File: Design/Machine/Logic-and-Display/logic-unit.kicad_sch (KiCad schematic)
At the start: 10 parts, among them J2 RJ45, K1 SRD-12VDC-SL-C, K2 SRD-12VDC-SL-C, K3 SRD-12VDC-SL-C, K4 SRD-12VDC-SL-C, SW1 ToggleAutoPoints, SW2 SynchRemote, U4 ESP32_NODEMCU, U5 NRF24L01_Breakout

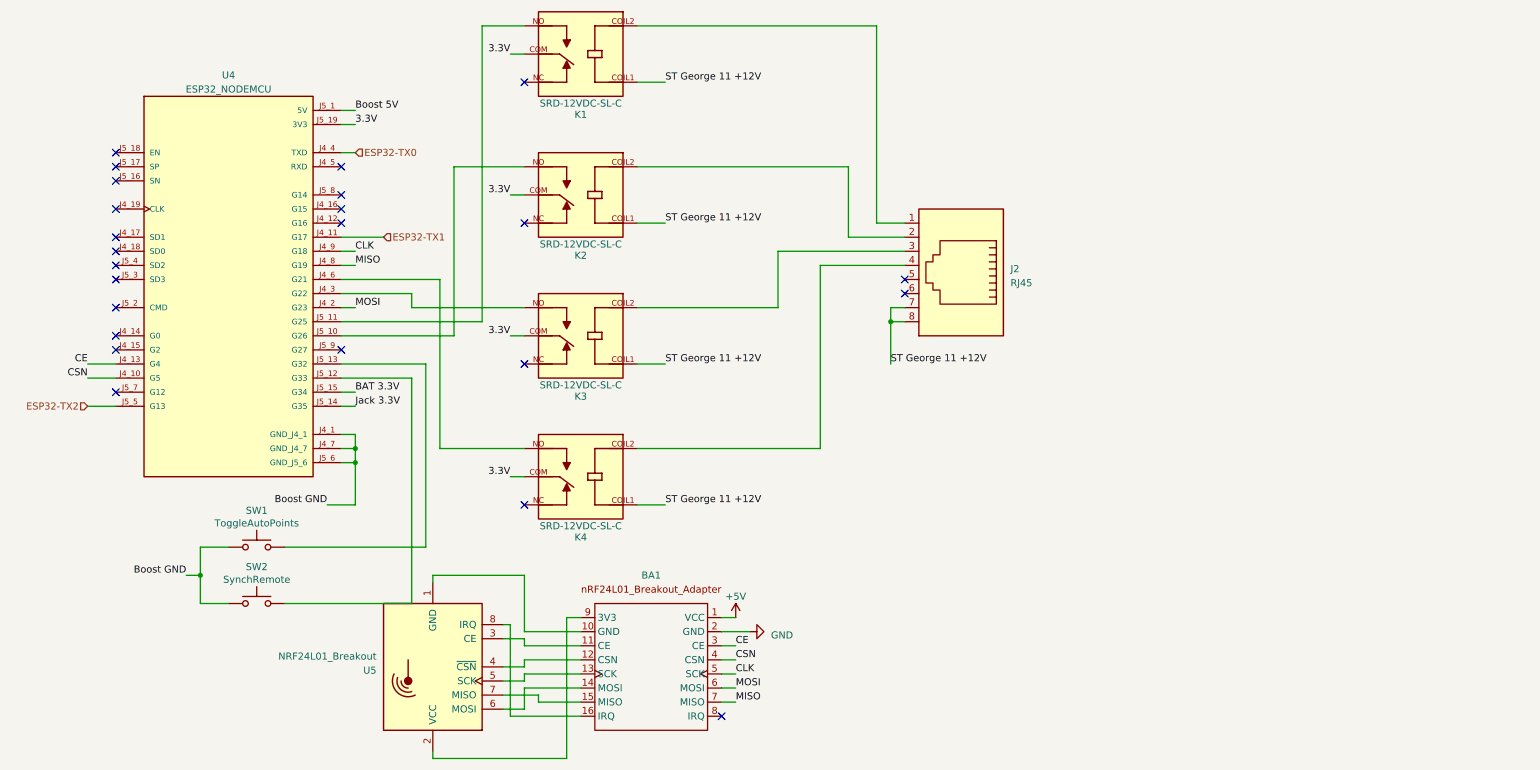
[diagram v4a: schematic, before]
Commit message: feat: logic and display units schecmatics
complete logic and display units schematics
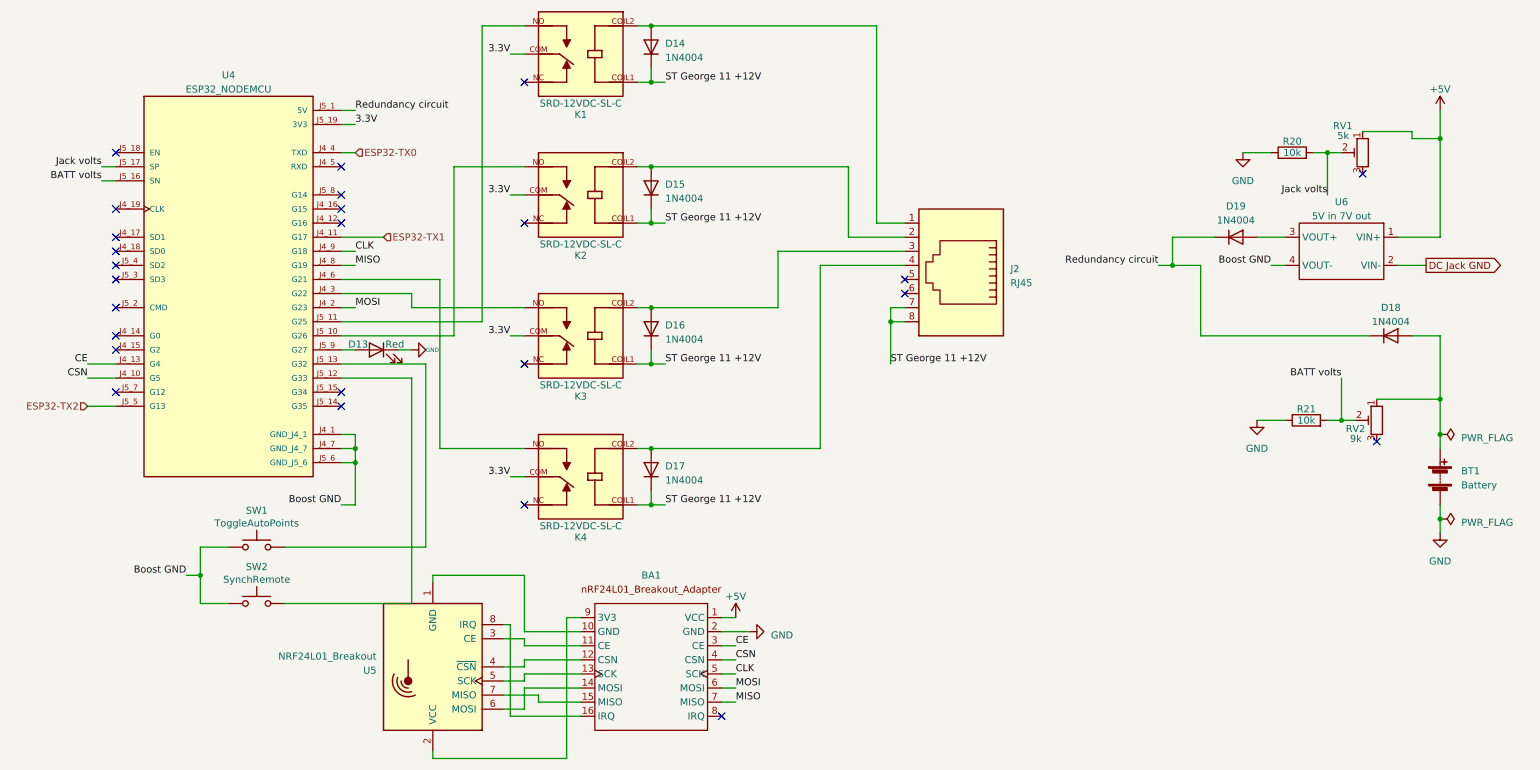
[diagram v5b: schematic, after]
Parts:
- added BT1: Battery, Connector_PinSocket_2.54mm:PinSocket_1x02_P2.54mm_Vertical, symbol Device:Battery
- added D13: Red, Connector_PinSocket_2.54mm:PinSocket_1x02_P2.54mm_Vertical, symbol Device:LED
- added D14, D15, D16, D17, D18, D19: 1N4004, Diode_THT:D_DO-41_SOD81_P10.16mm_Horizontal, symbol Diode:1N4004
- added R20, R21: 10k, Resistor_THT:R_Axial_DIN0309_L9.0mm_D3.2mm_P15.24mm_Horizontal, symbol Device:R
- added RV1: 5k, Connector_PinSocket_2.54mm:PinSocket_1x03_P2.54mm_Vertical, symbol Device:R_Potentiometer_Trim
- added RV2: 9k, Connector_PinSocket_2.54mm:PinSocket_1x03_P2.54mm_Vertical, symbol Device:R_Potentiometer_Trim
- added U6: 5V in 7V out, Connector_PinHeader_2.54mm:PinHeader_1x04_P2.54mm_Vertical, symbol Arduino modules:MT3608_step_up
- SW1, SW2: footprint Button_Switch_THT:SW_PUSH_6mm -> Connector_PinSocket_2.54mm:PinSocket_1x02_P2.54mm_Vertical
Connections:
- net +5V: now also RV1.1, U6.1 (VIN+)
- net Boost GND: now also U6.4 (VOUT-)
- net GND: now also BT1.2 (-), D13.1 (K), R20.1, R21.1
- net ST George 11 +12V: now also D14.1 (K), D15.1 (K), D16.1 (K), D17.1 (K)
- net at J2.1, K1.COIL2: now also D14.2 (A)
- net at J2.4, K4.COIL2: now also D17.2 (A)
- net BATT volts: now reaches U4.J5_16 (SN)
- net BATT volts: now also R21.2, RV2.2
- net Jack volts: now reaches U4.J5_17 (SP)
- net Jack volts: now also R20.2, RV1.2
- net at U4.J5_9 (G27): now also D13.2 (A)
- net at J2.2, K2.COIL2: now also D15.2 (A)
- net at J2.3, K3.COIL2: now also D16.2 (A)
- net BAT 3.3V: no longer names the net of U4.J5_15 (G34)
- net Boost 5V renamed Redundancy circuit
- net Redundancy circuit: now also D18.1 (K), D19.1 (K)
- net Jack 3.3V: no longer names the net of U4.J5_14 (G35)
- new net: D19.2 (A), U6.3 (VOUT+)
- new net: BT1.1 (+), D18.2 (A), RV2.1
- new net DC Jack GND: U6.2 (VIN-)
- no-connect marks 24 -> 25

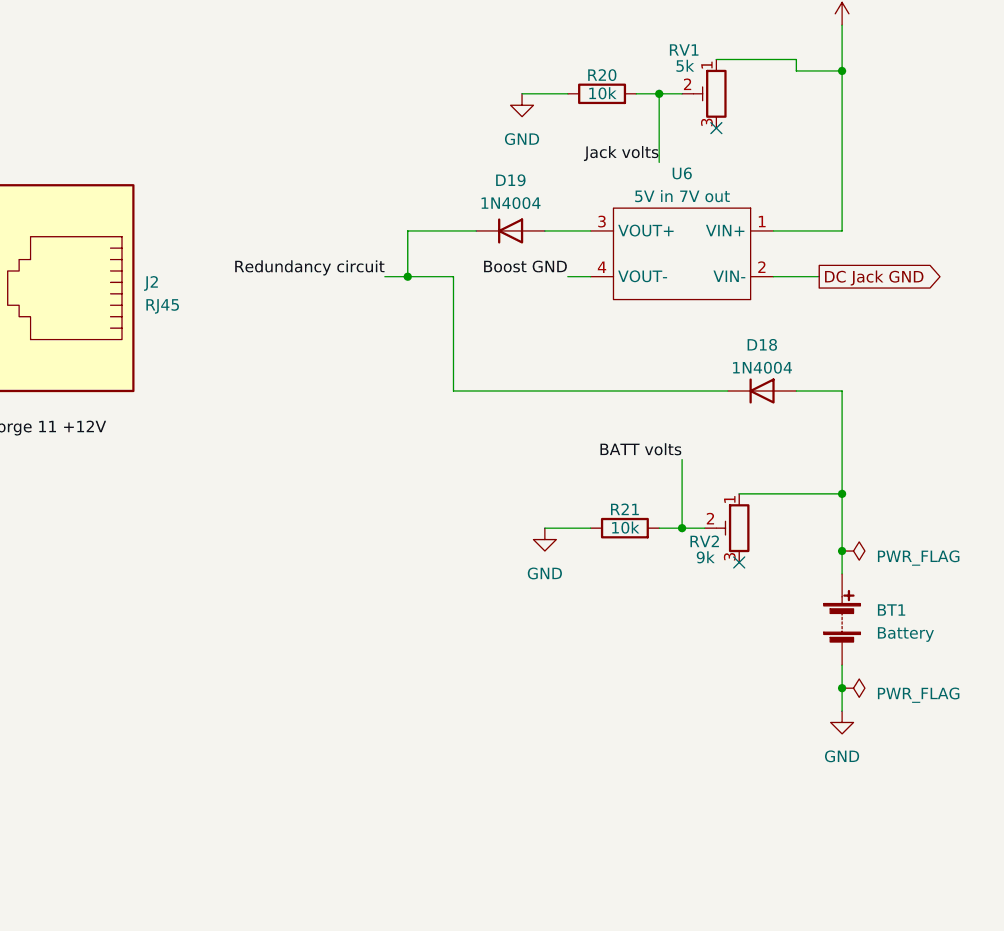
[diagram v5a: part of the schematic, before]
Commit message: fix: logic and display units on/off switch
include a DPST switch to disconnect battery and DC jack
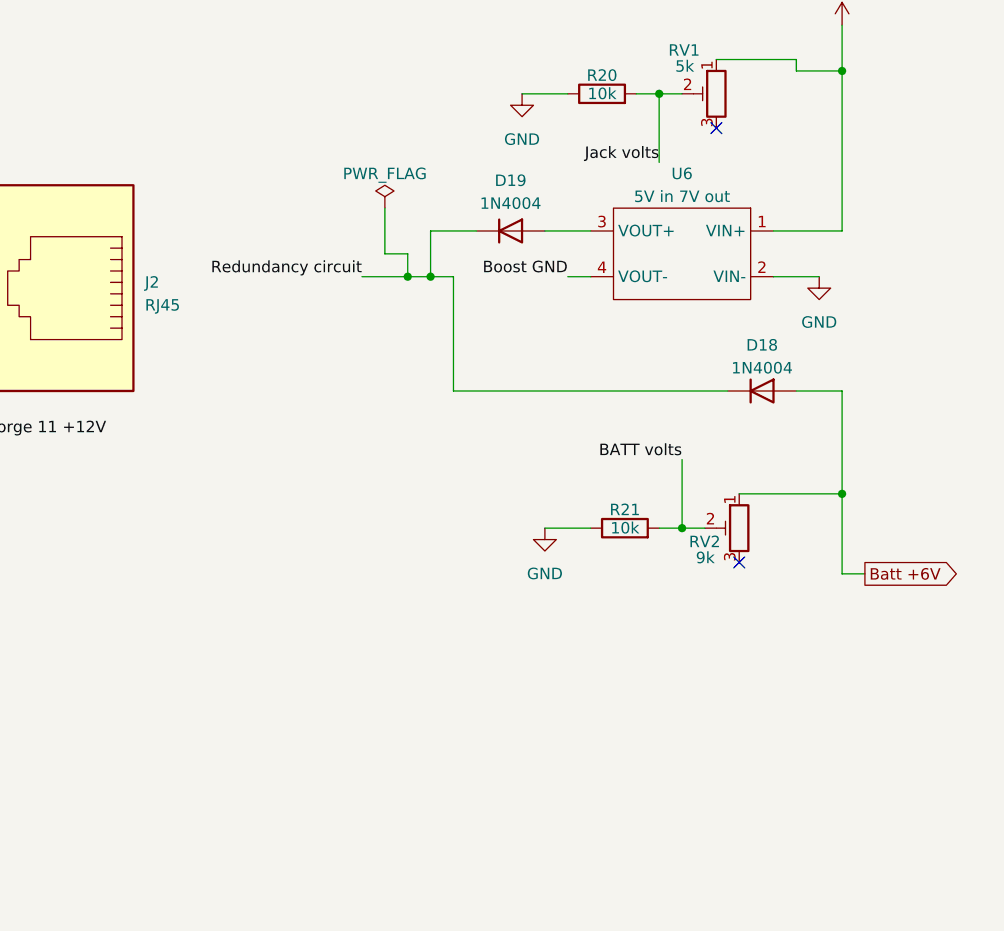
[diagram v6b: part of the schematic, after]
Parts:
- removed BT1: Battery, Connector_PinSocket_2.54mm:PinSocket_1x02_P2.54mm_Vertical, symbol Device:Battery
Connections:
- net DC Jack GND is gone; now on net GND: U6.2 (VIN-)
- net Batt +6V: now reaches D18.2 (A), RV2.1
